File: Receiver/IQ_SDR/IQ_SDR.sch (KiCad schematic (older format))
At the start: 99 parts, among them CON1 SJ1-3523N, J1 ANT, J10 LO_I, J11 LO_Q, J12 GNDA, J13 I_IN, J14 Q_IN, J15 +5V, J16 4.3V, J17 I_OUT, J18 Q_OUT, J19 Conn_01x01_Male, J2 GND, J20 Conn_01x01_Male, J3 V_IN pin header, J4 GND, J5 V_IN, J6 FIL_O, J7 CLK1, J8 CLK2, J9 CLK0, P1 BNC, P2 SMA, Q1 MMBT2222A-TP, T1 Transformer_1P_SS, T2 Transformer_1P_1S, U1 FST3253 or TS3A5017, U2 Si5351A-B-GT, U3 TS5A23157, U4 LM4562 or LT6231, U5 74ALVC74D, Y1 CX3225

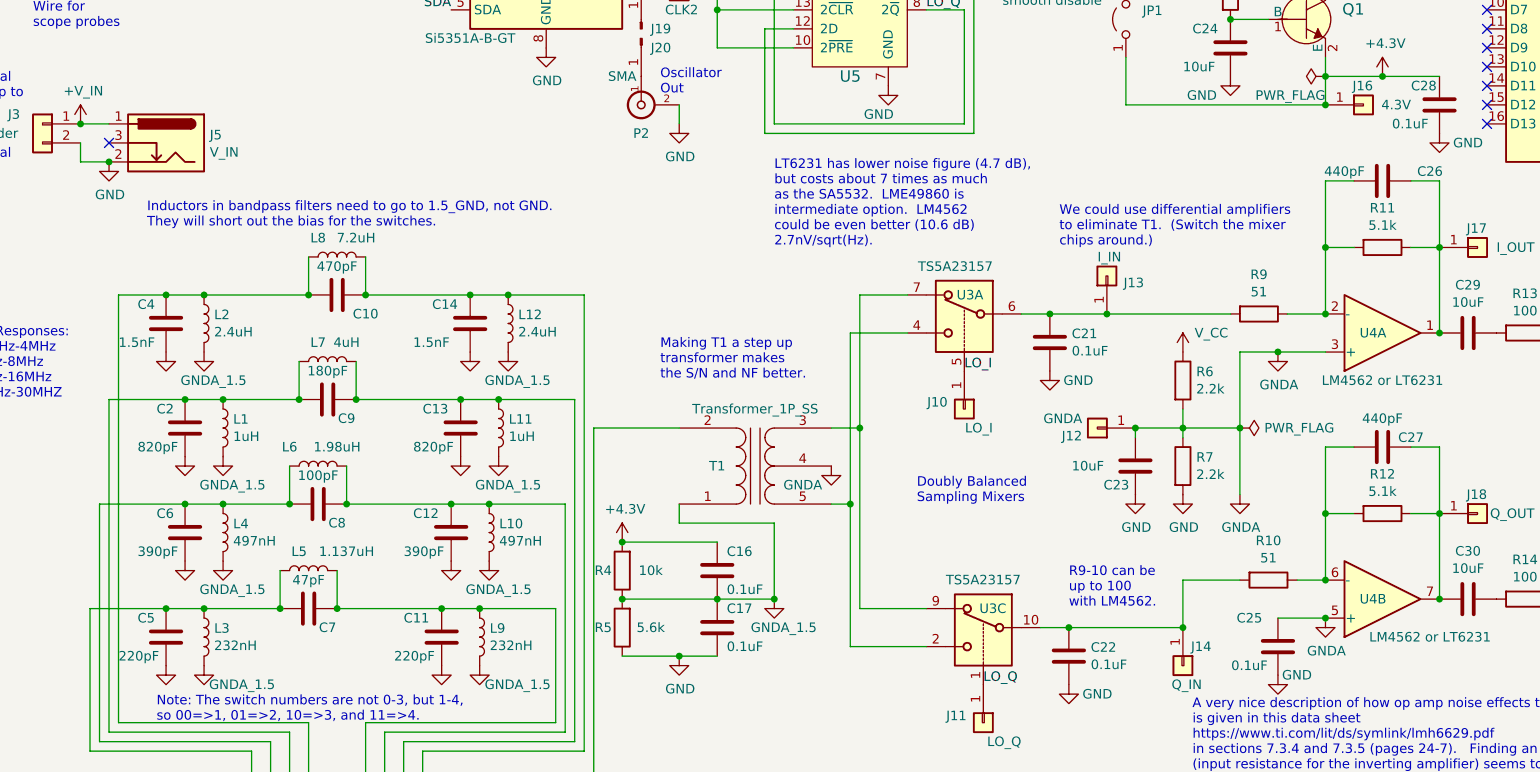
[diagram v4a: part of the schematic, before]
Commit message: Some errors in the bandpass filters and other places corrected to improve the sensitivity and ground loop noise.
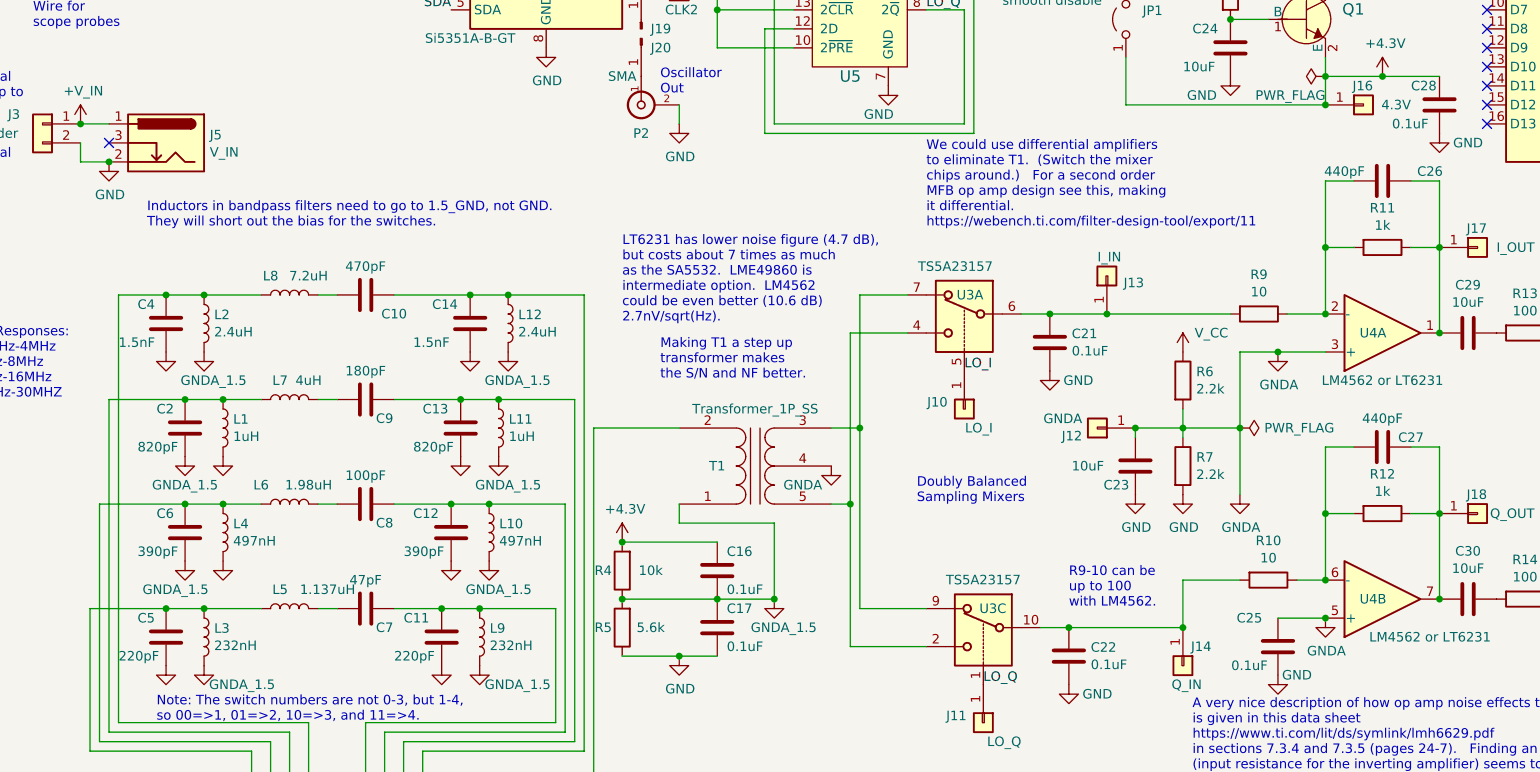
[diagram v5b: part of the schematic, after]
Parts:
- R10, R9: value 51 -> 10
- R11, R12: value 5.1k -> 1k
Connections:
- net at C4.1, L2.1, L8.1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: no longer C10.2
- net at C10.1, C14.1, L12.1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: no longer L8.2
- net at C11.1, C7.1, L9.1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: no longer L5.2
- net at C12.1, C8.1, L10.1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: no longer L6.2
- net at C13.1, C9.1, L11.1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: no longer L7.2
- net at C2.1, L1.1, L7.1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: no longer C9.2
- net at C6.1, L4.1, L6.1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: no longer C8.2
- net at C5.1, L3.1, L5.1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: no longer C7.2
- new net: C10.2, L8.2
- new net: C9.2, L7.2
- new net: C8.2, L6.2
- new net: C7.2, L5.2
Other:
- note added: "We could use differential amplifiers\nto eliminate T1. (Switch the mixer\nchips around.) For a second order\nMFB op amp design see this, making\nit differential. \nhttps://webench.ti.com/filter-design-tool/export/11"
- note removed: "We could use differential amplifiers\nto eliminate T1. (Switch the mixer\nchips around.)"
- moved on the sheet: C10, C7, C8, C9, L5, L6, L7, L8

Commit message: Added the LTSpice simulations and started on v0.20 changes.
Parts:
- removed L12: 2.4uH, Inductors_THT:L_Toroid_Vertical_L10.0mm_W5.0mm_P5.08mm, symbol IQ_SDR-rescue:L-Device
- added C33, C34, C35, C36, C38, C39, C40, C41, C42, C43, C44, C45, C46, C47, C48, C49: 1500pF, Capacitors_SMD:C_0805, symbol Device:C
- added C50, C51, C52: 0.1uF, symbol Device:C
- added JP5: Jumper, symbol Device:Jumper
- added L13, L14, L15, L16, L17, L18, L19, L20, L21, L22, L23, L24: 5.5uH, Inductors_THT:L_Toroid_Vertical_L10.0mm_W5.0mm_P5.08mm, symbol Device:L
- added Q2, Q3, Q4, Q5: 2N3904, Package_TO_SOT_THT:TO-92_Inline, symbol Transistor_BJT:2N3904
- added R17, R18: 100, symbol Device:R
- added R19, R20, R23, R24: 22, symbol Device:R
- added R21, R22: 1k, symbol Device:R
- added R25: R, symbol Device:R
- added R26, R27: 50, symbol Device:R
- added T3, T4: Transformer_SP_1S, symbol Device:Transformer_SP_1S
- C21, C22: value 0.1uF -> 0.02uF
- CON1: Sound Card Data (none) -> https://static.qobuz.com/info/IMG/pdf/VT1620A.pdf
- L10: value 497nH -> 626nH
- L11: value 1uH -> 1.7uH
- L9: value 232nH -> 256nH
- T1: Winding BN-43-2402, #30, primary 5\", seconday 2x3\" bifilar -> 2.4uH primary, trifilar wound 1:2 turns ratio
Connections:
- wire segments 219 -> 282
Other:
- note added: "We could use differential amplifiers. \n(Switch the mixer\nchips around.) For a second order\nMFB op amp design see this, making\nit differential. \nhttps://webench.ti.com/filter-design-tool/export/11"
- note removed: ".param freq=10000000"
- note removed: ".param if_freq={freq + 1000}"
- note removed: "Problems yet to solve:\nIn Quisk or maybe hardware, need to switch I and Q.\nOptional jumpers added to combat\nground loops without extra isolation."
- note removed: "We could use differential amplifiers\nto eliminate T1. (Switch the mixer\nchips around.) For a second order\nMFB op amp design see this, making\nit differential. \nhttps://webench.ti.com/filter-design-tool/export/11"
- moved on the sheet: A1, C15, C16, C17, C18, C19, C20, C21, C22, C23, C24, C25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

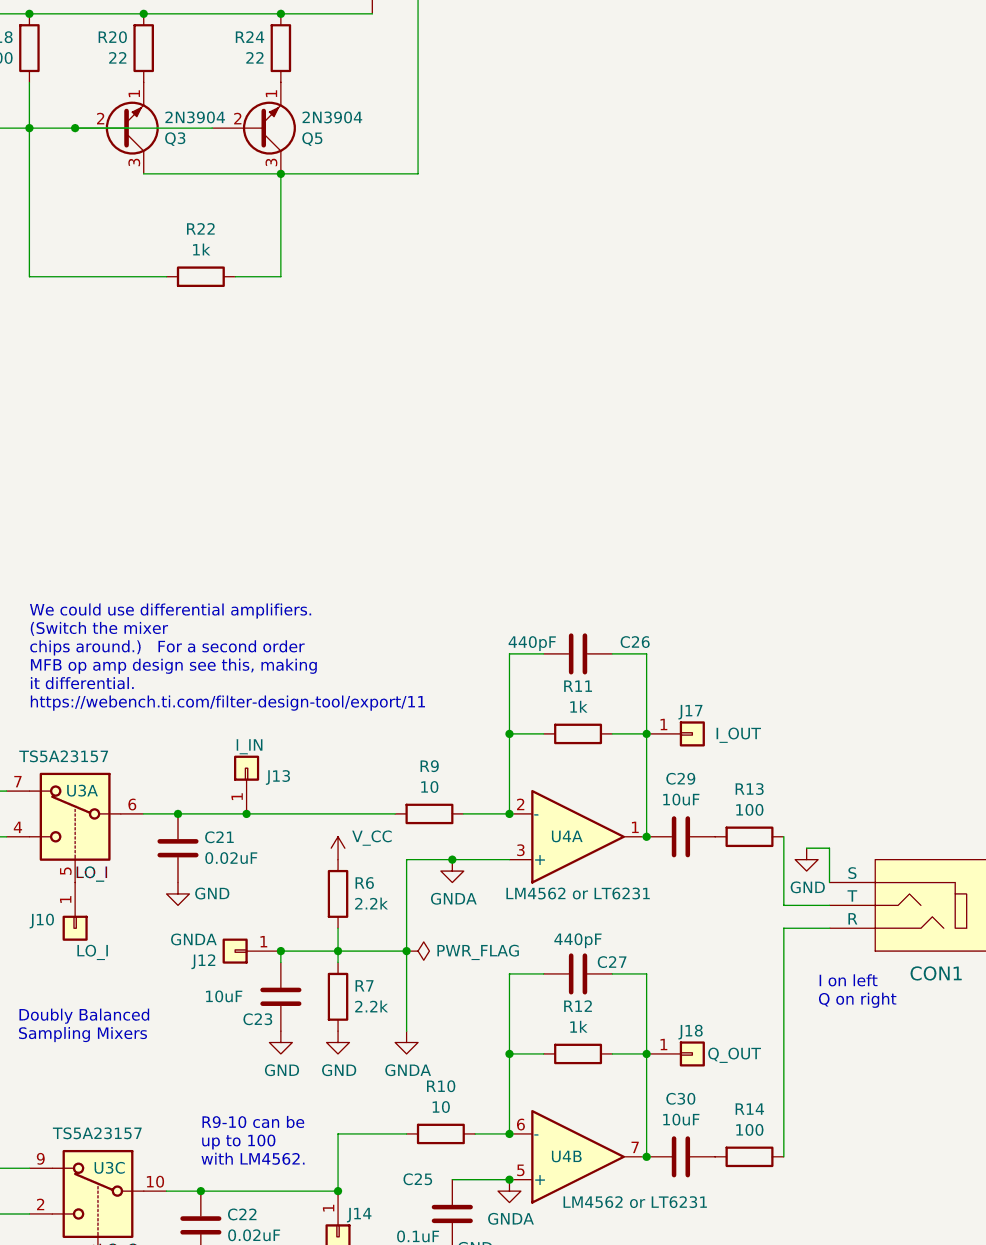
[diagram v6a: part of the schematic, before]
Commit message: Fixed some simulation file errors, especially with the noise simulation.
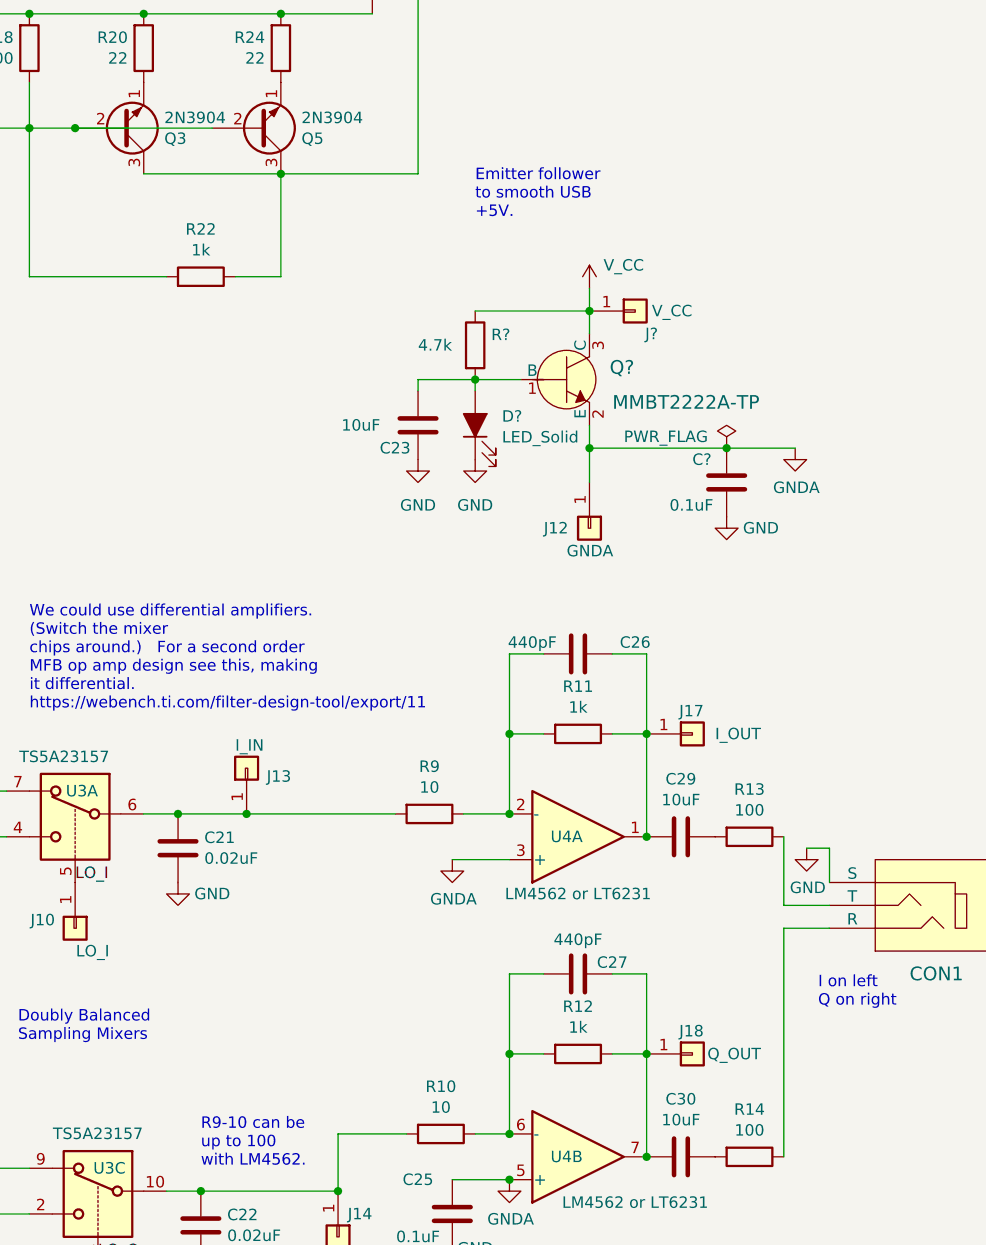
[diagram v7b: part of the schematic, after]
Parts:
- removed R6, R7: 2.2k, Resistors_SMD:R_0805, symbol IQ_SDR-rescue:R-Device
- added C?: 0.1uF, Capacitors_SMD:C_0805, symbol IQ_SDR-rescue:C-Device
- added D?: LED_Solid, symbol LED_Solid:LED_Solid
- added J?: V_CC, Connectors:PINTST, symbol IQ_SDR-rescue:Conn_01x01-Connector_Generic
- added Q?: MMBT2222A-TP, digikey-footprints:SOT-23-3, symbol IQ_SDR-rescue:MMBT2222A-TP-dk_Transistors-Bipolar-BJT-Single
- added R?: 4.7k, Resistors_SMD:R_0805, symbol IQ_SDR-rescue:R-Device
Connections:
- wire segments 282 -> 285
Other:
- moved on the sheet: C23, J12
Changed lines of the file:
@@
 NoConn ~ 15150 6500
 NoConn ~ 15150 6400
-$Comp
-L IQ_SDR-rescue:R-Device R6
-U 1 1 5CFD8143
-P 7450 7400
-F 0 "R6" H 7520 7446 50  0000 L CNN
-F 1 "2.2k" H 7520 7355 50  0000 L CNN
-F 2 "Resistors_SMD:R_0805" V 7380 7400 50  0001 C CNN
-F 3 "~" H 7450 7400 50  0001 C CNN
-	1    7450 7400
-	1    0    0    -1
-$EndComp
-$Comp
-L IQ_SDR-rescue:GND-power #PWR053
-U 1 1 5CFD92C7
-P 7450 8000
-F 0 "#PWR053" H 7450 7750 50  0001 C CNN
-F 1 "GND" H 7455 7827 50  0000 C CNN
-F 2 "" H 7450 8000 50  0001 C CNN
-F 3 "" H 7450 8000 50  0001 C CNN
-	1    7450 8000
-	1    0    0    -1
-$EndComp
-Wire Wire Line
-	7450 7700 7450 7650
-Wire Wire Line
-	7450 7650 7750 7650
-Connection ~ 7450 7650
 Wire Wire Line
-	7450 7650 7450 7550
-$Comp
-L IQ_SDR-rescue:R-Device R7
-U 1 1 5D491348
-P 7450 7850
-F 0 "R7" H 7520 7896 50  0000 L CNN
-F 1 "2.2k" H 7520 7805 50  0000 L CNN
-F 2 "Resistors_SMD:R_0805" V 7380 7850 50  0001 C CNN
-F 3 "~" H 7450 7850 50  0001 C CNN
-	1    7450 7850
-	1    0    0    -1
-$EndComp
-Wire Wire Line
-	7750 8000 7750 7650
-Wire Wire Line
-	7750 7250 7950 7250
-Connection ~ 7750 7650
+	8050 5200 8050 5150
+Connection ~ 8050 5150
 $Comp
 L IQ_SDR-rescue:C-Device C22
@@
 L IQ_SDR-rescue:C-Device C23
 U 1 1 5D043017
-P 7200 7850
-F 0 "C23" H 7300 7950 50  0000 C CNN
-F 1 "10uF" H 7450 7850 50  0000 C CNN
-F 2 "Capacitors_SMD:C_0805" H 7238 7700 50  0001 C CNN
-F 3 "~" H 7200 7850 50  0001 C CNN
-	1    7200 7850
+P 7800 5350
+F 0 "C23" H 7900 5450 50  0000 C CNN
+F 1 "10uF" H 8050 5350 50  0000 C CNN
+F 2 "Capacitors_SMD:C_0805" H 7838 5200 50  0001 C CNN
+F 3 "~" H 7800 5350 50  0001 C CNN
+	1    7800 5350
 	-1   0    0    1
 $EndComp
@@
 L IQ_SDR-rescue:GND-power #PWR051
 U 1 1 5D0438C2
-P 7200 8000
-F 0 "#PWR051" H 7200 7750 50  0001 C CNN
-F 1 "GND" H 7205 7827 50  0000 C CNN
-F 2 "" H 7200 8000 50  0001 C CNN
-F 3 "" H 7200 8000 50  0001 C CNN
-	1    7200 8000
+P 7800 5500
+F 0 "#PWR051" H 7800 5250 50  0001 C CNN
+F 1 "GND" H 7800 5300 50  0000 C CNN
+F 2 "" H 7800 5500 50  0001 C CNN
+F 3 "" H 7800 5500 50  0001 C CNN
+	1    7800 5500
 	1    0    0    -1
 $EndComp
 Wire Wire Line
-	7200 7700 7200 7650
+	7800 5200 7800 5150
 Wire Wire Line
-	7200 7650 7450 7650
+	7800 5150 8050 5150
 $Comp
 L IQ_SDR-rescue:C-Device C25
@@
 	9400 7450 9600 7450
 $Comp
-L IQ_SDR-rescue:PWR_FLAG-power #FLG02
-U 1 1 5D491365
-P 7750 7650
-F 0 "#FLG02" H 7750 7725 50  0001 C CNN
-F 1 "PWR_FLAG" V 7750 7778 50  0000 L CNN
-F 2 "" H 7750 7650 50  0001 C CNN
-F 3 "~" H 7750 7650 50  0001 C CNN
-F 4 "R" H 7750 7650 50  0001 C CNN "Spice_Primitive"
-F 5 "1" H 7750 7650 50  0001 C CNN "Spice_Model"
-F 6 "N" H 7750 7650 50  0001 C CNN "Spice_Netlist_Enabled"
-	1    7750 7650
-	0    1    1    0
-$EndComp
-$Comp
 L IQ_SDR-rescue:PWR_FLAG-power #FLG01
 U 1 1 5D491366
@@
 L IQ_SDR-rescue:Conn_01x01-Connector_Generic J12
 U 1 1 5D2AD39B
-P 7000 7650
-F 0 "J12" H 7080 7692 50  0000 L CNN
-F 1 "GNDA" H 7080 7601 50  0000 L CNN
-F 2 "Connectors:PINTST" H 7000 7650 50  0001 C CNN
-F 3 "~" H 7000 7650 50  0001 C CNN
-F 4 "J" H 7000 7650 50  0001 C CNN "Spice_Primitive"
-F 5 "Conn_01x01" H 7000 7650 50  0001 C CNN "Spice_Model"
-F 6 "N" H 7000 7650 50  0001 C CNN "Spice_Netlist_Enabled"
-	1    7000 7650
-	-1   0    0    1
+P 8550 5800
+F 0 "J12" V 8550 5600 50  0000 L CNN
+F 1 "GNDA" V 8650 5700 50  0000 L CNN
+F 2 "Connectors:PINTST" H 8550 5800 50  0001 C CNN
+F 3 "~" H 8550 5800 50  0001 C CNN
+F 4 "J" H 8550 5800 50  0001 C CNN "Spice_Primitive"
+F 5 "Conn_01x01" H 8550 5800 50  0001 C CNN "Spice_Model"
+F 6 "N" H 8550 5800 50  0001 C CNN "Spice_Netlist_Enabled"
+	1    8550 5800
+	0    1    1    0
 $EndComp
 Text Label 1550 7100 0    50   ~ 0
@@
 	1    0    0    -1
 $EndComp
-Connection ~ 7200 7650
-Wire Wire Line
-	7750 7250 7750 7650
 $Comp
 L IQ_SDR-rescue:C-Device C3
@@
 L lt6231:V_CC #PWR052
 U 1 1 5D237FD0
-P 7450 7250
-F 0 "#PWR052" H 7450 7100 50  0001 C CNN
-F 1 "V_CC" H 7600 7350 50  0000 C CNN
-F 2 "" H 7450 7250 50  0001 C CNN
-F 3 "" H 7450 7250 50  0001 C CNN
-	1    7450 7250
+P 8550 4750
+F 0 "#PWR052" H 8550 4600 50  0001 C CNN
+F 1 "V_CC" H 8700 4850 50  0000 C CNN
+F 2 "" H 8550 4750 50  0001 C CNN
+F 3 "" H 8550 4750 50  0001 C CNN
+	1    8550 4750
 	1    0    0    -1
 $EndComp
@@
 $EndComp
 $Comp
-L IQ_SDR-rescue:GNDA-power #PWR0111
-U 1 1 5E0B69D9
-P 7750 8000
-F 0 "#PWR0111" H 7750 7750 50  0001 C CNN
-F 1 "GNDA" H 7755 7827 50  0000 C CNN
-F 2 "" H 7750 8000 50  0001 C CNN
-F 3 "" H 7750 8000 50  0001 C CNN
-	1    7750 8000
-	1    0    0    -1
-$EndComp
-$Comp
 L IQ_SDR-rescue:GNDA-power #PWR0112
 U 1 1 5E0B6E6F
@@
 	1    0    0    -1
 $EndComp
-Connection ~ 7950 7250
 Wire Wire Line
 	7950 7250 8200 7250
@@
 Wire Wire Line
 	3700 3550 4300 3550
+$Comp
+L IQ_SDR-rescue:R-Device R?
+U 1 1 5E9FE9F4
+P 8050 5000
+F 0 "R?" H 8120 5046 50  0000 L CNN
+F 1 "4.7k" H 7800 5000 50  0000 L CNN
+F 2 "Resistors_SMD:R_0805" V 7980 5000 50  0001 C CNN
+F 3 "~" H 8050 5000 50  0001 C CNN
+	1    8050 5000
+	1    0    0    -1
+$EndComp
+Wire Wire Line
+	8550 4850 8550 4950
+Wire Wire Line
+	8550 5350 8550 5450
+$Comp
+L IQ_SDR-rescue:GND-power #PWR?
+U 1 1 5E9FEA03
+P 8050 5500
+F 0 "#PWR?" H 8050 5250 50  0001 C CNN
+F 1 "GND" H 8050 5300 50  0000 C CNN
+F 2 "" H 8050 5500 50  0001 C CNN
+F 3 "" H 8050 5500 50  0001 C CNN
+	1    8050 5500
+	1    0    0    -1
+$EndComp
+$Comp
+L IQ_SDR-rescue:Conn_01x01-Connector_Generic J?
+U 1 1 5E9FEA0C
+P 8750 4850
+F 0 "J?" H 8850 4750 50  0000 R CNN
+F 1 "V_CC" H 9000 4850 50  0000 R CNN
+F 2 "Connectors:PINTST" H 8750 4850 50  0001 C CNN
+F 3 "~" H 8750 4850 50  0001 C CNN
+F 4 "J" H 8750 4850 50  0001 C CNN "Spice_Primitive"
+F 5 "Conn_01x01" H 8750 4850 50  0001 C CNN "Spice_Model"
+F 6 "N" H 8750 4850 50  0001 C CNN "Spice_Netlist_Enabled"
+	1    8750 4850
+	1    0    0    -1
+$EndComp
+Wire Wire Line
+	8550 5600 8550 5450
+Connection ~ 8550 5450
+$Comp
+L IQ_SDR-rescue:C-Device C?
+U 1 1 5E9FEA1D
+P 9150 5600
+F 0 "C?" H 9000 5700 50  0000 L CNN
+F 1 "0.1uF" H 8900 5500 50  0000 L CNN
+F 2 "Capacitors_SMD:C_0805" H 9188 5450 50  0001 C CNN
+F 3 "~" H 9150 5600 50  0001 C CNN
+	1    9150 5600
+	1    0    0    -1
+$EndComp
+$Comp
+L IQ_SDR-rescue:GND-power #PWR?
+U 1 1 5E9FEA23
+P 9150 5750
+F 0 "#PWR?" H 9150 5500 50  0001 C CNN
+F 1 "GND" H 9300 5700 50  0000 C CNN
+F 2 "" H 9150 5750 50  0001 C CNN
+F 3 "" H 9150 5750 50  0001 C CNN
+	1    9150 5750
+	1    0    0    -1
+$EndComp
+$Comp
+L IQ_SDR-rescue:MMBT2222A-TP-dk_Transistors-Bipolar-BJT-Single Q?
+U 1 1 5E9FEA32
+P 8450 5150
+F 0 "Q?" H 8638 5203 60  0000 L CNN
+F 1 "MMBT2222A-TP" H 8650 5050 60  0000 L CNN
+F 2 "digikey-footprints:SOT-23-3" H 8650 5350 60  0001 L CNN
+F 3 "https://www.mouser.com/datasheet/2/308/MMBT2222A-1301352.pdf" H 8650 5450 60  0001 L CNN
+F 4 "MMBT2222ATPMSCT-ND" H 8650 5550 60  0001 L CNN "Digi-Key_PN"
+F 5 "MMBT2222A-TP" H 8650 5650 60  0001 L CNN "MPN"
+F 6 "Discrete Semiconductor Products" H 8650 5750 60  0001 L CNN "Category"
+F 7 "Transistors - Bipolar (BJT) - Single" H 8650 5850 60  0001 L CNN "Family"
+F 8 "http://www.mccsemi.com/up_pdf/MMBT2222A(SOT-23).pdf" H 8650 5950 60  0001 L CNN "DK_Datasheet_Link"
+F 9 "/product-detail/en/micro-commercial-co/MMBT2222A-TP/MMBT2222ATPMSCT-ND/717394" H 8650 6050 60  0001 L CNN "DK_Detail_Page"
+F 10 "TRANS NPN 40V 0.6A SOT23" H 8650 6150 60  0001 L CNN "Description"
+F 11 "Micro Commercial Co" H 8650 6250 60  0001 L CNN "Manufacturer"
+F 12 "Active" H 8650 6350 60  0001 L CNN "Status"
+	1    8450 5150
+	1    0    0    -1
+$EndComp
+Wire Wire Line
+	8050 5150 8250 5150
+Wire Wire Line
+	8050 4850 8550 4850
+$Comp
+L IQ_SDR-rescue:PWR_FLAG-power #FLG?
+U 1 1 5E9FEA3B
+P 9150 5450
+F 0 "#FLG?" H 9150 5525 50  0001 C CNN
+F 1 "PWR_FLAG" H 8700 5500 50  0000 L CNN
+F 2 "" H 9150 5450 50  0001 C CNN
+F 3 "~" H 9150 5450 50  0001 C CNN
+	1    9150 5450
+	1    0    0    -1
+$EndComp
+Wire Wire Line
+	8550 4750 8550 4850
+Connection ~ 8550 4850
+Text Notes 8050 4450 0    50   ~ 0
+Emitter follower\nto smooth USB\n+5V.
+Wire Wire Line
+	8550 5450 9150 5450
+$Comp
+L LED_Solid:LED_Solid D?
+U 1 1 5EB0C444
+P 8050 5350
+F 0 "D?" V 8089 5233 50  0000 R CNN
+F 1 "LED_Solid" V 7998 5233 50  0000 R CNN
+F 2 "" H 8050 5350 50  0001 C CNN
+F 3 "~" H 8050 5350 50  0001 C CNN
+	1    8050 5350
+	0    -1   -1   0
+$EndComp
+Connection ~ 9150 5450
+$Comp
+L IQ_SDR-rescue:GNDA-power #PWR?
+U 1 1 5EB0E2E2
+P 9450 5450
+F 0 "#PWR?" H 9450 5200 50  0001 C CNN
+F 1 "GNDA" H 9455 5277 50  0000 C CNN
+F 2 "" H 9450 5450 50  0001 C CNN
+F 3 "" H 9450 5450 50  0001 C CNN
+	1    9450 5450
+	1    0    0    -1
+$EndComp
+Wire Wire Line
+	9150 5450 9450 5450
 $EndSCHEMATC
